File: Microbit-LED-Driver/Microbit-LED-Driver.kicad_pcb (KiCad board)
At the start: 2 copper layers, 60 x 52 mm, 21 parts, among them J1 Conn_01x02_Socket, J2 Conn_01x02_Socket, J3 Conn_01x02_Socket, Q1 BCP56, Q2 BCP56, Q3 BCP56

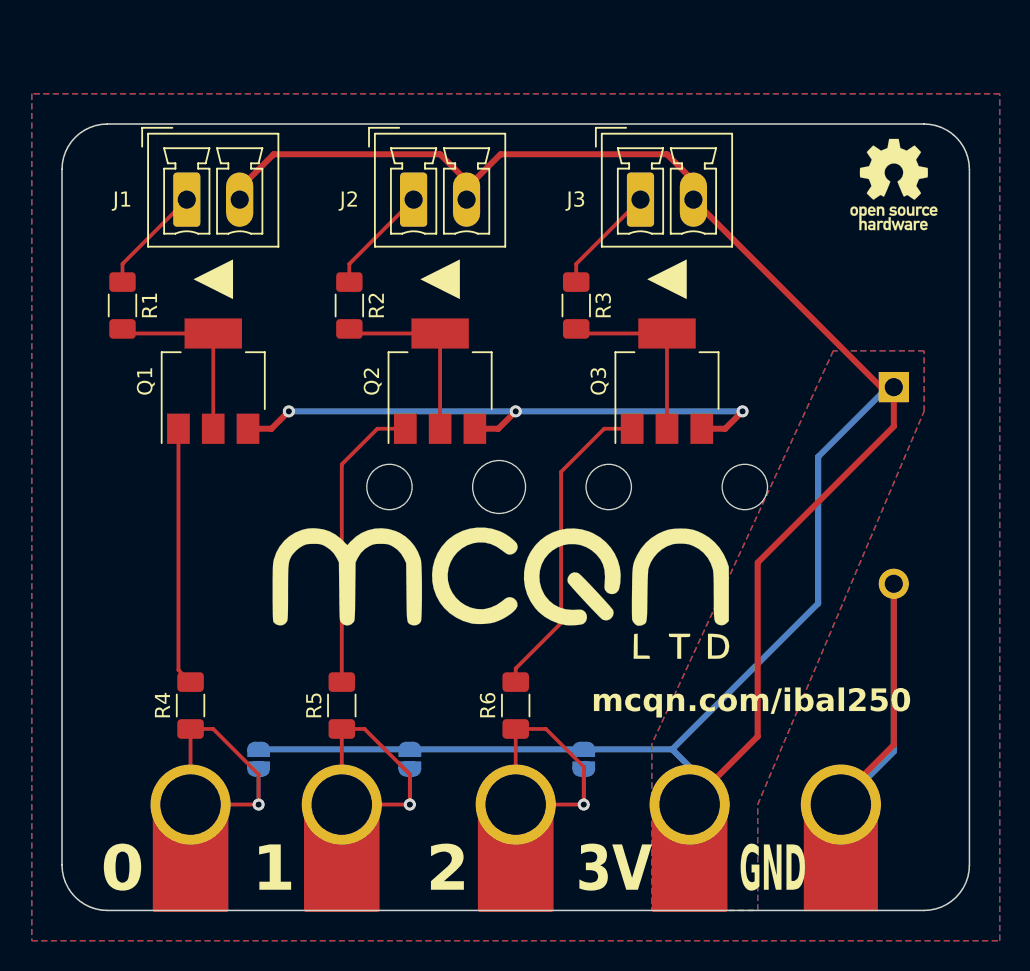
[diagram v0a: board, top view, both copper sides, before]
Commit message: Nugde position of screw terminals and battery holder so they shouldn't clash.  Fixes #3
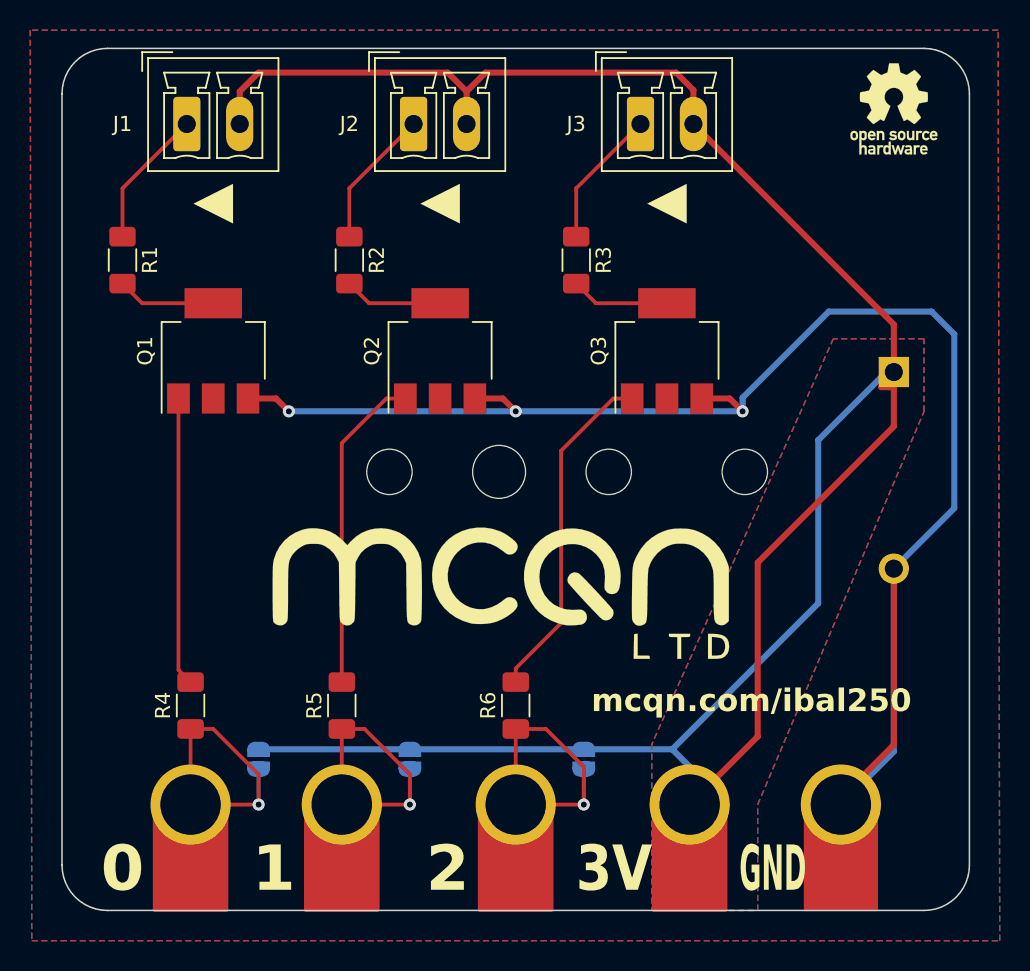
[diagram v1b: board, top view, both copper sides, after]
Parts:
- moved J1 5.00 mm to (78.2, 24.0)
- moved J2 5.00 mm to (93.2, 24.0)
- moved J3 5.00 mm to (108.2, 24.0)
- moved REF** 5.00 mm to (125.0, 23.0)
- moved REF** 5.00 mm to (74.0, 23.0)
- moved R1 3.00 mm to (74.0, 33.0)
- moved R2 3.00 mm to (89.0, 33.0)
- moved R3 3.00 mm to (104.0, 33.0)
- moved Q1 2.00 mm to (80.0, 39.0)
- moved Q2 2.00 mm to (95.0, 39.0)
- moved Q3 2.00 mm to (110.0, 39.0)
- moved BT1 1.00 mm to (125.0, 40.4)
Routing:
- net GND: track 71.2 -> 107.8 mm
- net +3V0: track 150.8 -> 158.9 mm
- net Net-(Q3-C-Pad2): track 12.4 -> 6.54 mm
- net Net-(Q2-C-Pad2): track 12.4 -> 6.54 mm
- net Net-(Q1-C-Pad2): track 12.4 -> 6.54 mm
- net Net-(Q1-B): track 17.1 -> 19.1 mm
- net Net-(J3-Pin_1): track 7.21 -> 9.21 mm
- net Net-(J2-Pin_1): track 7.21 -> 9.21 mm
- net Net-(J1-Pin_1): track 7.21 -> 9.21 mm
- net Net-(Q3-B): track 21.0 -> 22.7 mm
- net Net-(Q2-B): track 19.6 -> 21.2 mm
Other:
- board size 60 x 52 mm -> 60 x 57 mm
- board text added: "r20241021"
- board text removed: "r20240916"
